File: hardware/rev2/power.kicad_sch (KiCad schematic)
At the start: 20 parts, among them U5 MP2664GG-xxxx-P, U6 MAX17055ETB+, U7 TPS63805YFFR

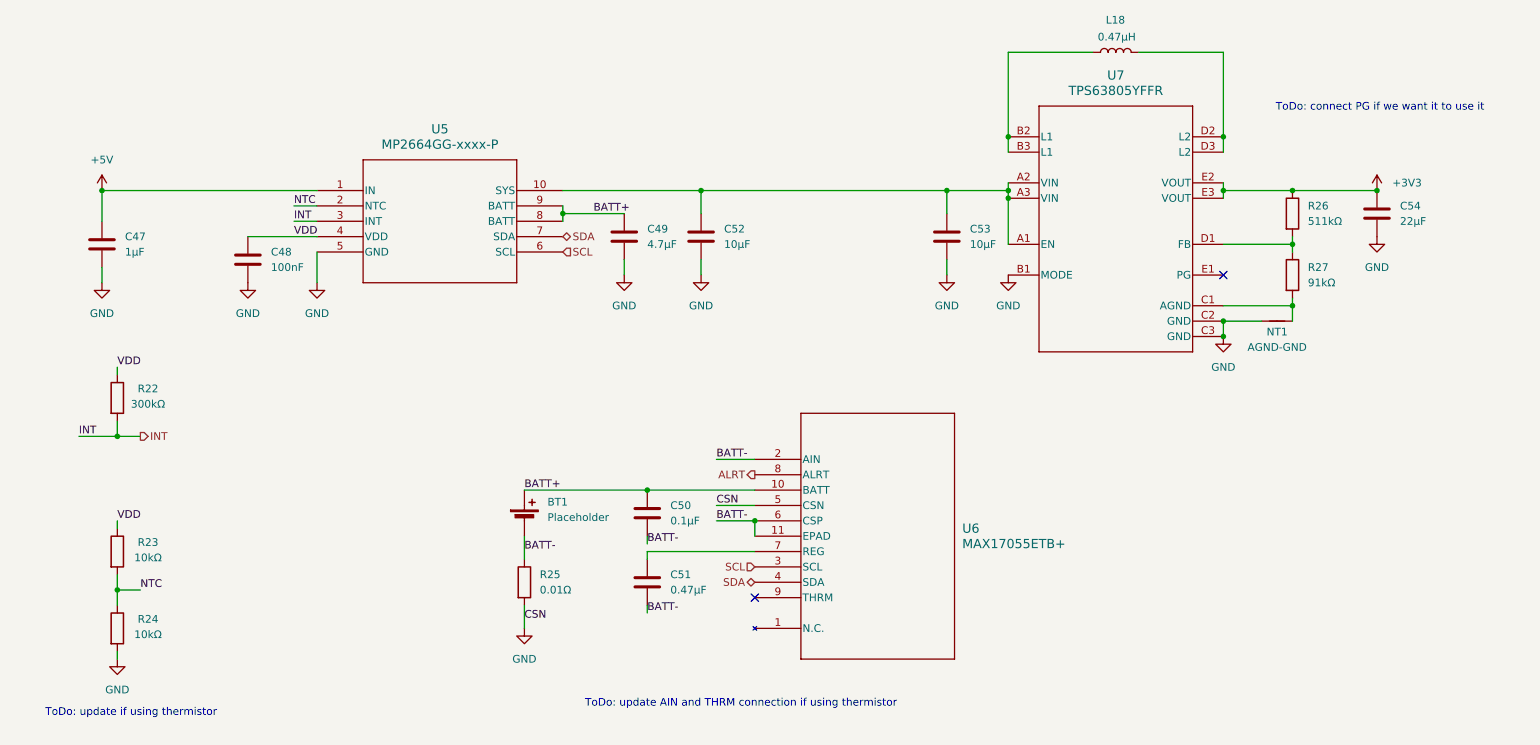
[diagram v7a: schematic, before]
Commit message: routed everything ESP32 and SX1262, will hopefully work. still needs more testpoints
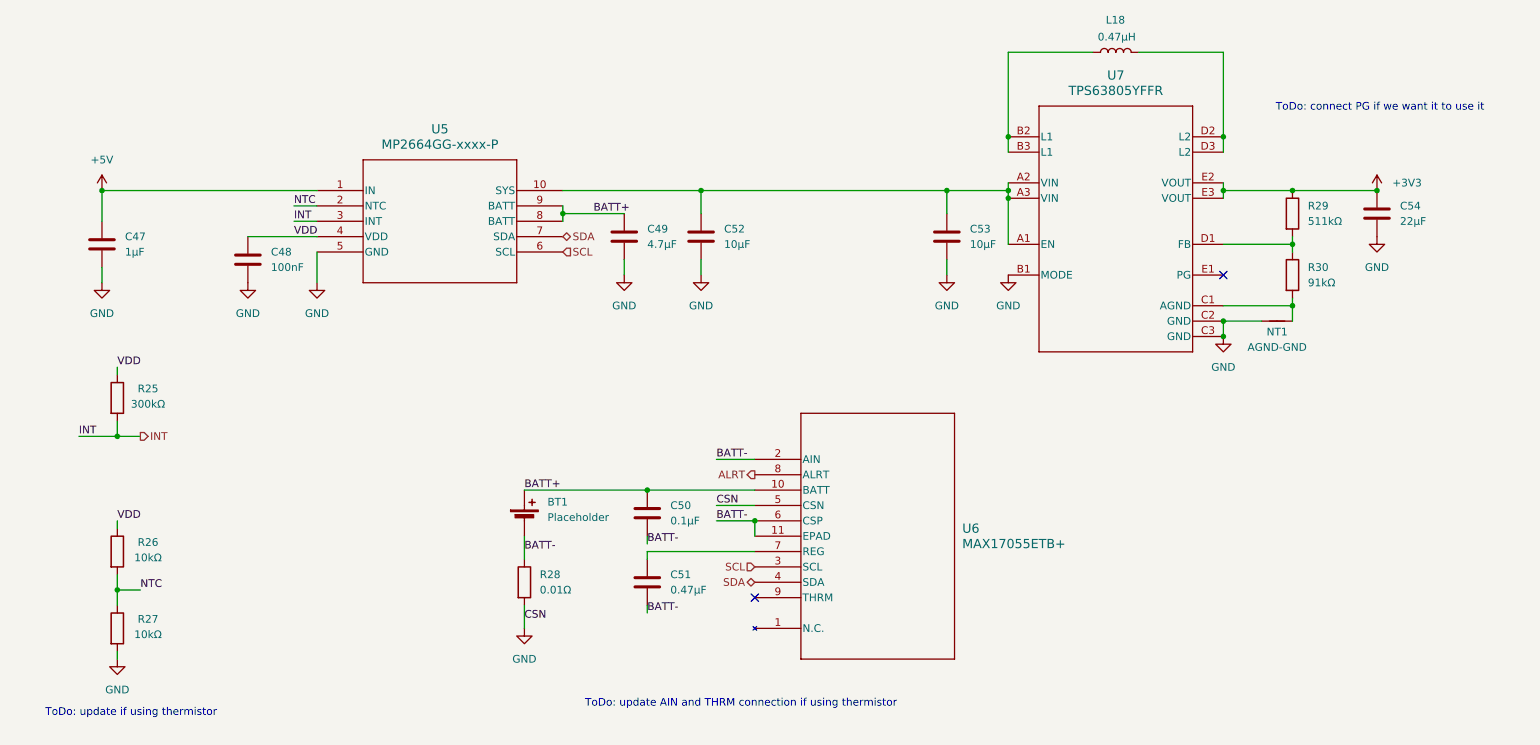
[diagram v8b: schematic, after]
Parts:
- U5: footprint QFN-2x2_MP2664_MNP -> _footprints:QFN-2x2_MP2664_MNP
- U6: footprint 21-100013A_T102A2+1C_MXM -> _footprints:21-100013A_T102A2+1C_MXM
- U7: footprint YFF0015AHAN -> _footprints:YFF0015AHAN
- renumbered R22 to R25, R23 to R26, R24 to R27, R25 to R28, R26 to R29, R27 to R30
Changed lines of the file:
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@@
 		(dnp no)
 		(fields_autoplaced yes)
-		(property "Reference" "#PWR075"
+		(property "Reference" "#PWR074"
 			(at 53.34 96.52 0)
 			(hide yes)
@@
 			(project "rev2"
 				(path "/9067f306-e23c-4d77-8182-4fa2c4b88902/46484475-7656-401a-9d45-159f5e421427"
-					(reference "#PWR075")
+					(reference "#PWR074")
 					(unit 1)
 				)
@@
 		(dnp no)
 		(fields_autoplaced yes)
-		(property "Reference" "#PWR078"
+		(property "Reference" "#PWR077"
 			(at 115.57 95.25 0)
 			(hide yes)
@@
 			(project "rev2"
 				(path "/9067f306-e23c-4d77-8182-4fa2c4b88902/46484475-7656-401a-9d45-159f5e421427"
-					(reference "#PWR078")
+					(reference "#PWR077")
 					(unit 1)
 				)
@@
 		(dnp no)
 		(fields_autoplaced yes)
-		(property "Reference" "#PWR079"
+		(property "Reference" "#PWR078"
 			(at 128.27 95.25 0)
 			(hide yes)
@@
 			(project "rev2"
 				(path "/9067f306-e23c-4d77-8182-4fa2c4b88902/46484475-7656-401a-9d45-159f5e421427"
-					(reference "#PWR079")
+					(reference "#PWR078")
 					(unit 1)
 				)
@@
 		(dnp no)
 		(fields_autoplaced yes)
-		(property "Reference" "#PWR073"
+		(property "Reference" "#PWR072"
 			(at 29.21 96.52 0)
 			(hide yes)
@@
 			(project "rev2"
 				(path "/9067f306-e23c-4d77-8182-4fa2c4b88902/46484475-7656-401a-9d45-159f5e421427"
-					(reference "#PWR073")
+					(reference "#PWR072")
 					(unit 1)
 				)
@@
 			)
 		)
-		(property "Footprint" "QFN-2x2_MP2664_MNP"
+		(property "Footprint" "_footprints:QFN-2x2_MP2664_MNP"
 			(at 64.77 74.93 0)
 			(hide yes)
@@
 		(in_pos_files yes)
 		(dnp no)
-		(property "Reference" "R23"
+		(property "Reference" "R26"
 			(at 36.83 133.096 0)
 			(show_name no)
@@
 			(project "rev2"
 				(path "/9067f306-e23c-4d77-8182-4fa2c4b88902/46484475-7656-401a-9d45-159f5e421427"
-					(reference "R23")
+					(reference "R26")
 					(unit 1)
 				)
@@
 		(dnp no)
 		(fields_autoplaced yes)
-		(property "Reference" "#PWR080"
+		(property "Reference" "#PWR079"
 			(at 168.91 95.25 0)
 			(hide yes)
@@
 			(project "rev2"
 				(path "/9067f306-e23c-4d77-8182-4fa2c4b88902/46484475-7656-401a-9d45-159f5e421427"
-					(reference "#PWR080")
+					(reference "#PWR079")
 					(unit 1)
 				)
@@
 		(dnp no)
 		(fields_autoplaced yes)
-		(property "Reference" "#PWR084"
+		(property "Reference" "#PWR083"
 			(at 240.03 88.9 0)
 			(hide yes)
@@
 			(project "rev2"
 				(path "/9067f306-e23c-4d77-8182-4fa2c4b88902/46484475-7656-401a-9d45-159f5e421427"
-					(reference "#PWR084")
+					(reference "#PWR083")
 					(unit 1)
 				)
@@
 		(dnp no)
 		(fields_autoplaced yes)
-		(property "Reference" "R26"
+		(property "Reference" "R29"
 			(at 228.6 77.4699 0)
 			(show_name no)
@@
 			(project "rev2"
 				(path "/9067f306-e23c-4d77-8182-4fa2c4b88902/46484475-7656-401a-9d45-159f5e421427"
-					(reference "R26")
+					(reference "R29")
 					(unit 1)
 				)
@@
 			)
 		)
-		(property "Footprint" "YFF0015AHAN"
+		(property "Footprint" "_footprints:YFF0015AHAN"
 			(at 196.85 81.28 0)
 			(hide yes)
@@
 			)
 		)
-		(property "Footprint" "21-100013A_T102A2+1C_MXM"
+		(property "Footprint" "_footprints:21-100013A_T102A2+1C_MXM"
 			(at 137.16 119.38 0)
 			(hide yes)
@@
 		(in_pos_files yes)
 		(dnp no)
-		(property "Reference" "R22"
+		(property "Reference" "R25"
 			(at 36.83 107.696 0)
 			(show_name no)
@@
 			(project "rev2"
 				(path "/9067f306-e23c-4d77-8182-4fa2c4b88902/46484475-7656-401a-9d45-159f5e421427"
-					(reference "R22")
+					(reference "R25")
 					(unit 1)
 				)
@@
 		(dnp no)
 		(fields_autoplaced yes)
-		(property "Reference" "#PWR077"
+		(property "Reference" "#PWR076"
 			(at 99.06 153.67 0)
 			(hide yes)
@@
 			(project "rev2"
 				(path "/9067f306-e23c-4d77-8182-4fa2c4b88902/46484475-7656-401a-9d45-159f5e421427"
-					(reference "#PWR077")
+					(reference "#PWR076")
 					(unit 1)
 				)
@@
 		(in_pos_files yes)
 		(dnp no)
-		(property "Reference" "R24"
+		(property "Reference" "R27"
 			(at 36.83 145.796 0)
 			(show_name no)
@@
 			(project "rev2"
 				(path "/9067f306-e23c-4d77-8182-4fa2c4b88902/46484475-7656-401a-9d45-159f5e421427"
-					(reference "R24")
+					(reference "R27")
 					(unit 1)
 				)
@@
 		(dnp no)
 		(fields_autoplaced yes)
-		(property "Reference" "#PWR082"
+		(property "Reference" "#PWR081"
 			(at 214.63 105.41 0)
 			(hide yes)
@@
 			(project "rev2"
 				(path "/9067f306-e23c-4d77-8182-4fa2c4b88902/46484475-7656-401a-9d45-159f5e421427"
-					(reference "#PWR082")
+					(reference "#PWR081")
 					(unit 1)
 				)
@@
 		(dnp no)
 		(fields_autoplaced yes)
-		(property "Reference" "#PWR076"
+		(property "Reference" "#PWR075"
 			(at 64.77 96.52 0)
 			(hide yes)
@@
 			(project "rev2"
 				(path "/9067f306-e23c-4d77-8182-4fa2c4b88902/46484475-7656-401a-9d45-159f5e421427"
-					(reference "#PWR076")
+					(reference "#PWR075")
 					(unit 1)
 				)
@@
 		(dnp no)
 		(fields_autoplaced yes)
-		(property "Reference" "#PWR072"
+		(property "Reference" "#PWR071"
 			(at 29.21 78.74 0)
 			(hide yes)
@@
 			(project "rev2"
 				(path "/9067f306-e23c-4d77-8182-4fa2c4b88902/46484475-7656-401a-9d45-159f5e421427"
-					(reference "#PWR072")
+					(reference "#PWR071")
 					(unit 1)
 				)
@@
 		(dnp no)
 		(fields_autoplaced yes)
-		(property "Reference" "#PWR074"
+		(property "Reference" "#PWR073"
 			(at 31.75 158.75 0)
 			(hide yes)
@@
 			(project "rev2"
 				(path "/9067f306-e23c-4d77-8182-4fa2c4b88902/46484475-7656-401a-9d45-159f5e421427"
-					(reference "#PWR074")
+					(reference "#PWR073")
 					(unit 1)
 				)
@@
 		(dnp no)
 		(fields_autoplaced yes)
-		(property "Reference" "#PWR083"
+		(property "Reference" "#PWR082"
 			(at 240.03 78.74 0)
 			(hide yes)
@@
 			(project "rev2"
 				(path "/9067f306-e23c-4d77-8182-4fa2c4b88902/46484475-7656-401a-9d45-159f5e421427"
-					(reference "#PWR083")
+					(reference "#PWR082")
 					(unit 1)
 				)
@@
 		(dnp no)
 		(fields_autoplaced yes)
-		(property "Reference" "#PWR081"
+		(property "Reference" "#PWR080"
 			(at 179.07 95.25 0)
 			(hide yes)
@@
 			(project "rev2"
 				(path "/9067f306-e23c-4d77-8182-4fa2c4b88902/46484475-7656-401a-9d45-159f5e421427"
-					(reference "#PWR081")
+					(reference "#PWR080")
 					(unit 1)
 				)
@@
 		(dnp no)
 		(fields_autoplaced yes)
-		(property "Reference" "R27"
+		(property "Reference" "R30"
 			(at 228.6 87.6299 0)
 			(show_name no)
@@
 			(project "rev2"
 				(path "/9067f306-e23c-4d77-8182-4fa2c4b88902/46484475-7656-401a-9d45-159f5e421427"
-					(reference "R27")
+					(reference "R30")
 					(unit 1)
 				)
@@
 		(dnp no)
 		(fields_autoplaced yes)
-		(property "Reference" "R25"
+		(property "Reference" "R28"
 			(at 101.6 138.4299 0)
 			(show_name no)
@@
 			(project "rev2"
 				(path "/9067f306-e23c-4d77-8182-4fa2c4b88902/46484475-7656-401a-9d45-159f5e421427"
-					(reference "R25")
-					(unit 1)
-				)
+					(reference "R28")
+					(unit 1)
+				)
